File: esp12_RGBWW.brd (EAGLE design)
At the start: 53 x 47 mm, 36 parts, among them Q1 AOD2910SMD, Q2 AOD2910SMD, Q3 AOD2910SMD, Q4 AOD2910SMD, Q5 AOD2910SMD, U1 TPS5410DR

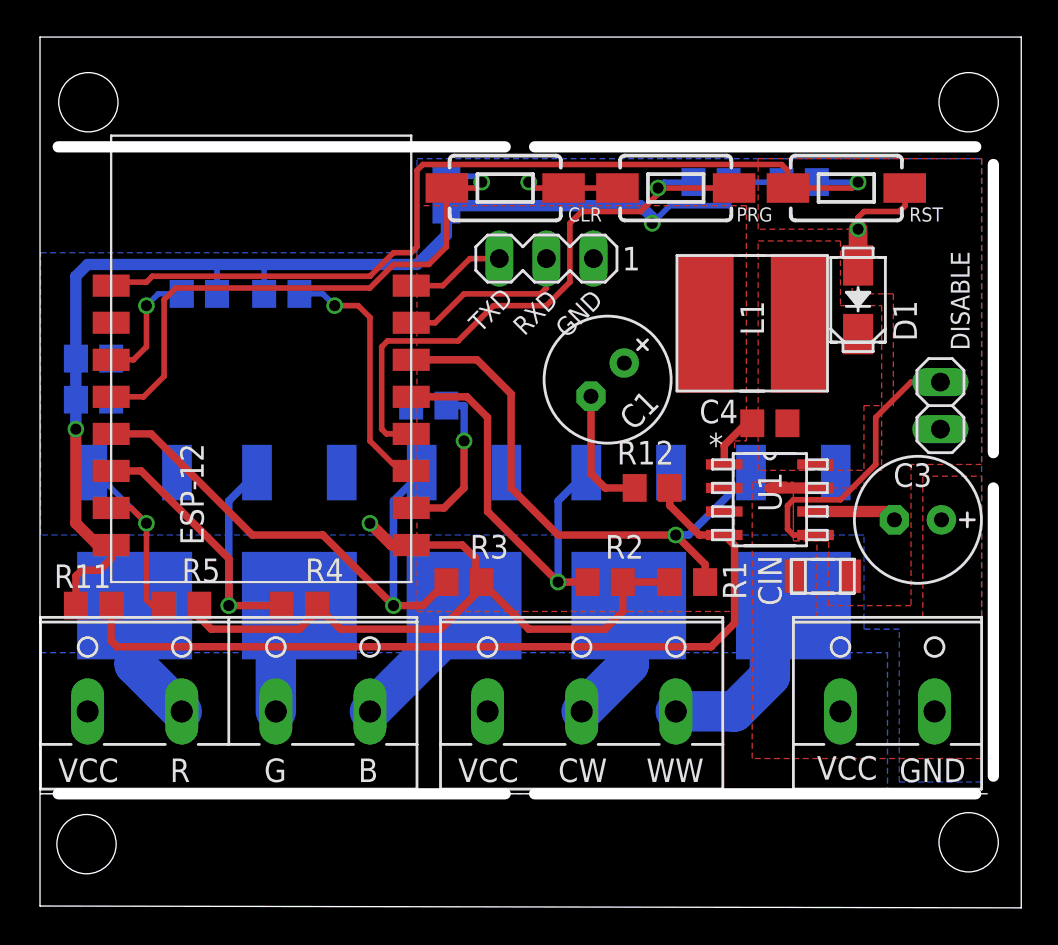
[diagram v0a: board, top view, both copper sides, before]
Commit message: minor routing changes
updated a few minor routings (clr) and added some more copper areas (GND around DISABLE & D1)
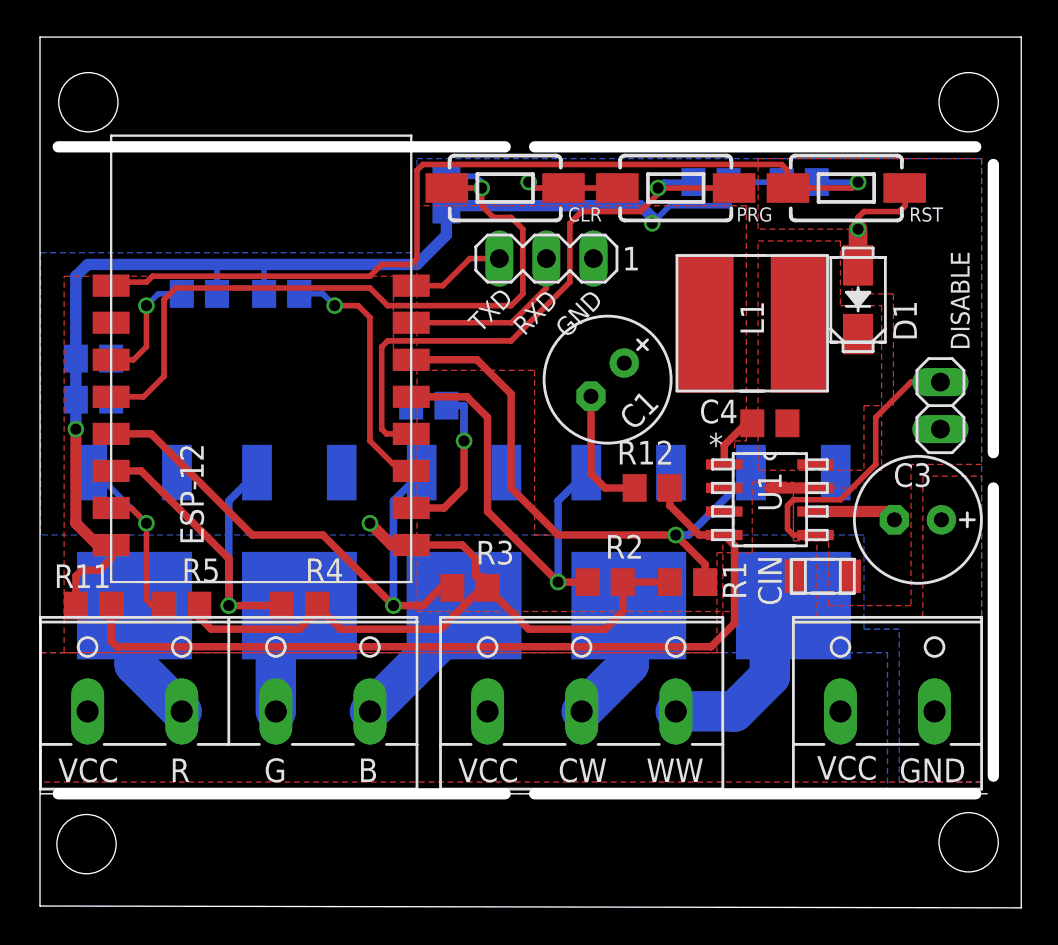
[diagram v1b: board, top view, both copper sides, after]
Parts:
- moved R3 0.45 mm to (21.9, 11.1)
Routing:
- net CLR_S: track 31.6 -> 39.4 mm
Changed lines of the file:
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@@
 <attribute name="NAME" x="29.21" y="12.7" size="1.27" layer="25"/>
 </element>
-<element name="R3" library="rcl" package="R0805" value="10k" x="21.59" y="11.43" smashed="yes">
-<attribute name="NAME" x="21.9075" y="12.7" size="1.27" layer="25"/>
+<element name="R3" library="rcl" package="R0805" value="10k" x="21.9075" y="11.1125" smashed="yes">
+<attribute name="NAME" x="22.225" y="12.3825" size="1.27" layer="25"/>
 </element>
 <element name="R4" library="rcl" package="R0805" value="10k" x="12.7" y="10.16" smashed="yes">
@@
 <wire x1="17.145" y1="19.685" x2="17.145" y2="24.13" width="0.3048" layer="1"/>
 <wire x1="17.145" y1="24.13" x2="17.4625" y2="24.4475" width="0.3048" layer="1"/>
-<wire x1="17.4625" y1="24.4475" x2="21.2725" y2="24.4475" width="0.3048" layer="1"/>
+<wire x1="17.4625" y1="24.4475" x2="24.13" y2="24.4475" width="0.3048" layer="1"/>
 <wire x1="27.305" y1="27.6225" x2="27.305" y2="30.7975" width="0.3048" layer="1"/>
 <wire x1="27.305" y1="30.7975" x2="27.94" y2="31.4325" width="0.3048" layer="1"/>
@@
 <wire x1="32.385" y1="33.02" x2="32.0675" y2="32.7025" width="0.3048" layer="16"/>
 <wire x1="36.17" y1="32.7025" x2="32.0675" y2="32.7025" width="0.3048" layer="1"/>
-<wire x1="21.2725" y1="24.4475" x2="23.1775" y2="26.3525" width="0.3048" layer="1"/>
-<wire x1="23.1775" y1="26.3525" x2="26.035" y2="26.3525" width="0.3048" layer="1"/>
-<wire x1="26.035" y1="26.3525" x2="27.305" y2="27.6225" width="0.3048" layer="1"/>
+<wire x1="24.13" y1="24.4475" x2="27.305" y2="27.6225" width="0.3048" layer="1"/>
 </signal>
 <signal name="GND">
@@
 <vertex x="-1.27" y="13.97"/>
 </polygon>
-<wire x1="22.54" y1="11.75" x2="22.54" y2="11.43" width="0.4064" layer="1"/>
-<wire x1="22.54" y1="11.43" x2="22.54" y2="11.11" width="0.4064" layer="1"/>
+<wire x1="22.54" y1="11.75" x2="22.8575" y2="11.1125" width="0.4064" layer="1"/>
+<wire x1="22.8575" y1="11.1125" x2="22.54" y2="11.11" width="0.4064" layer="1"/>
 <wire x1="22.54" y1="11.11" x2="20.32" y2="8.89" width="0.4064" layer="1"/>
 <wire x1="20.32" y1="8.89" x2="14.92" y2="8.89" width="0.4064" layer="1"/>
-<wire x1="22.54" y1="11.43" x2="22.86" y2="11.43" width="0.4064" layer="1"/>
+<wire x1="22.8575" y1="11.1125" x2="22.86" y2="11.43" width="0.4064" layer="1"/>
 <contactref element="VCC" pad="2"/>
 <contactref element="PROG" pad="1"/>
 <via x="16.51" y="14.605" extent="1-16" drill="0.6"/>
-<wire x1="25.08" y1="8.89" x2="22.54" y2="11.43" width="0.4064" layer="1"/>
+<wire x1="25.08" y1="8.89" x2="22.8575" y2="11.1125" width="0.4064" layer="1"/>
 <wire x1="18.74" y1="13.43" x2="21.495" y2="13.43" width="0.4064" layer="1"/>
 <wire x1="21.495" y1="13.43" x2="22.225" y2="12.7" width="0.4064" layer="1"/>
 <wire x1="22.225" y1="12.7" x2="22.225" y2="11.745" width="0.4064" layer="1"/>
-<wire x1="22.225" y1="11.745" x2="22.54" y2="11.43" width="0.4064" layer="1"/>
+<wire x1="22.225" y1="11.745" x2="22.8575" y2="11.1125" width="0.4064" layer="1"/>
 <wire x1="14.92" y1="8.89" x2="13.65" y2="10.16" width="0.4064" layer="1"/>
 <wire x1="13.65" y1="10.16" x2="13.65" y2="9.84" width="0.4064" layer="1"/>
@@
 <wire x1="40.5638" y1="15.24" x2="44.37295625" y2="15.24" width="0.6096" layer="1"/>
 <wire x1="44.37295625" y1="15.24" x2="44.821971875" y2="14.790984375" width="0.6096" layer="1"/>
+<polygon width="0.4064" layer="1">
+<vertex x="0" y="27.94"/>
+<vertex x="17.78" y="27.94"/>
+<vertex x="17.78" y="22.86"/>
+<vertex x="25.4" y="22.86"/>
+<vertex x="25.4" y="13.97"/>
+<vertex x="35.56" y="13.97"/>
+<vertex x="35.56" y="7.62"/>
+<vertex x="0" y="7.62"/>
+</polygon>
 </signal>
 <signal name="RST_S" class="5">
@@
 <wire x1="2.7325" y1="27.6225" x2="2.54" y2="27.43" width="0.3048" layer="1"/>
 <wire x1="40.6375" y1="33.02" x2="42.8625" y2="33.02" width="0.3048" layer="16"/>
-<wire x1="16.51" y1="27.94" x2="17.78" y2="29.21" width="0.3048" layer="1"/>
-<wire x1="17.78" y1="29.21" x2="18.7325" y2="29.21" width="0.3048" layer="1"/>
-<wire x1="18.7325" y1="29.21" x2="19.05" y2="29.5275" width="0.3048" layer="1"/>
 <wire x1="39.0775" y1="32.7025" x2="42.545" y2="32.7025" width="0.3048" layer="1"/>
 <wire x1="42.545" y1="32.7025" x2="42.8625" y2="33.02" width="0.3048" layer="1"/>
-<wire x1="19.05" y1="29.5275" x2="19.05" y2="33.655" width="0.3048" layer="1"/>
 <wire x1="19.05" y1="33.655" x2="19.3675" y2="33.9725" width="0.3048" layer="1"/>
 <wire x1="19.3675" y1="33.9725" x2="38.735" y2="33.9725" width="0.3048" layer="1"/>
@@
 <wire x1="39.0525" y1="33.655" x2="39.0525" y2="32.7275" width="0.3048" layer="1"/>
 <wire x1="39.0525" y1="32.7275" x2="39.0775" y2="32.7025" width="0.3048" layer="1"/>
+<wire x1="16.51" y1="27.94" x2="17.145" y2="28.575" width="0.3048" layer="1"/>
+<wire x1="17.145" y1="28.575" x2="18.7325" y2="28.575" width="0.3048" layer="1"/>
+<wire x1="18.7325" y1="28.575" x2="19.05" y2="28.8925" width="0.3048" layer="1"/>
+<wire x1="19.05" y1="28.8925" x2="19.05" y2="33.655" width="0.3048" layer="1"/>
 </signal>
 <signal name="RXD">
 <contactref element="ESP-12" pad="7"/>
 <contactref element="PROG" pad="2"/>
-<wire x1="18.74" y1="25.43" x2="20.0325" y2="25.43" width="0.3048" layer="1"/>
-<wire x1="20.0325" y1="25.43" x2="21.59" y2="26.9875" width="0.3048" layer="1"/>
-<wire x1="21.59" y1="26.9875" x2="25.7175" y2="26.9875" width="0.3048" layer="1"/>
-<wire x1="25.7175" y1="26.9875" x2="26.035" y2="27.305" width="0.3048" layer="1"/>
+<wire x1="18.74" y1="25.43" x2="24.16" y2="25.43" width="0.3048" layer="1"/>
+<wire x1="24.16" y1="25.43" x2="26.035" y2="27.305" width="0.3048" layer="1"/>
 <wire x1="26.035" y1="27.305" x2="26.035" y2="28.8925" width="0.3048" layer="1"/>
 </signal>
@@
 <contactref element="Q3" pad="1"/>
 <via x="17.78" y="10.16" extent="1-16" drill="0.6"/>
-<wire x1="20.64" y1="11.43" x2="19.37" y2="10.16" width="0.4064" layer="1"/>
 <wire x1="19.37" y1="10.16" x2="17.78" y2="10.16" width="0.4064" layer="1"/>
 <wire x1="10.16" y1="13.97" x2="4.7" y2="19.43" width="0.4064" layer="1"/>
@@
 <wire x1="17.78" y1="10.16" x2="17.78" y2="15.816" width="0.4064" layer="16"/>
 <wire x1="17.78" y1="15.816" x2="19.304" y2="17.34" width="0.4064" layer="16"/>
+<wire x1="19.37" y1="10.16" x2="19.37" y2="10.1625" width="0.4064" layer="1"/>
+<wire x1="19.37" y1="10.1625" x2="20.32" y2="11.1125" width="0.4064" layer="1"/>
+<wire x1="20.32" y1="11.1125" x2="20.9575" y2="11.1125" width="0.4064" layer="1"/>
 </signal>
 <signal name="RGB-G">
@@
 <vertex x="46.355" y="17.145"/>
 <vertex x="49.53" y="17.145"/>
-<vertex x="49.53" y="1.905"/>
-<vertex x="37.1475" y="1.905"/>
+<vertex x="49.53" y="0.635"/>
+<vertex x="-1.27" y="0.635"/>
+<vertex x="-1.27" y="7.62"/>
+<vertex x="35.2425" y="7.62"/>
+<vertex x="35.2425" y="13.0175"/>
+<vertex x="37.1475" y="13.0175"/>
 </polygon>
 <wire x1="40.5638" y1="16.51" x2="38.1" y2="16.51" width="0.6096" layer="1"/>
@@
 <contactref element="CLR" pad="2"/>
 <wire x1="2.38" y1="21.59" x2="2.54" y2="21.43" width="0.3048" layer="1"/>
-<wire x1="20.6375" y1="32.995" x2="20.6625" y2="32.7025" width="0.3048" layer="1"/>
-<via x="22.5425" y="33.02" extent="1-16" drill="0.6"/>
+<via x="22.5425" y="32.7025" extent="1-16" drill="0.6"/>
 <wire x1="20.6375" y1="33.335" x2="22.2275" y2="33.335" width="0.3048" layer="16"/>
-<wire x1="22.2275" y1="33.335" x2="22.5425" y2="33.02" width="0.3048" layer="16"/>
 <wire x1="2.54" y1="21.43" x2="4.285" y2="21.43" width="0.3048" layer="1"/>
 <wire x1="4.285" y1="21.43" x2="5.3975" y2="22.5425" width="0.3048" layer="1"/>
@@
 <wire x1="6.0325" y1="27.305" x2="5.3975" y2="26.67" width="0.3048" layer="1"/>
 <wire x1="5.3975" y1="26.67" x2="5.3975" y2="22.5425" width="0.3048" layer="1"/>
-<wire x1="16.51" y1="27.305" x2="17.78" y2="28.575" width="0.3048" layer="1"/>
-<wire x1="17.78" y1="28.575" x2="19.685" y2="28.575" width="0.3048" layer="1"/>
-<wire x1="19.685" y1="28.575" x2="20.6375" y2="29.5275" width="0.3048" layer="1"/>
-<wire x1="20.6375" y1="29.5275" x2="20.6375" y2="32.6775" width="0.3048" layer="1"/>
 <wire x1="20.6375" y1="32.6775" x2="20.6625" y2="32.7025" width="0.3048" layer="1"/>
-<wire x1="20.6625" y1="32.7025" x2="22.225" y2="32.7025" width="0.3048" layer="1"/>
-<wire x1="22.225" y1="32.7025" x2="22.5425" y2="33.02" width="0.3048" layer="1"/>
+<wire x1="16.51" y1="27.305" x2="17.4625" y2="26.3525" width="0.3048" layer="1"/>
+<wire x1="17.4625" y1="26.3525" x2="24.13" y2="26.3525" width="0.3048" layer="1"/>
+<wire x1="24.13" y1="26.3525" x2="24.765" y2="26.9875" width="0.3048" layer="1"/>
+<wire x1="24.765" y1="26.9875" x2="24.765" y2="30.48" width="0.3048" layer="1"/>
+<wire x1="22.2275" y1="33.335" x2="22.5425" y2="33.02" width="0.3048" layer="16"/>
+<wire x1="22.5425" y1="33.02" x2="22.5425" y2="32.7025" width="0.3048" layer="16"/>
+<wire x1="20.6625" y1="32.7025" x2="22.5425" y2="32.7025" width="0.3048" layer="1"/>
+<wire x1="22.5425" y1="32.7025" x2="22.5425" y2="31.75" width="0.3048" layer="1"/>
+<wire x1="22.5425" y1="31.75" x2="23.1775" y2="31.115" width="0.3048" layer="1"/>
+<wire x1="23.1775" y1="31.115" x2="24.13" y2="31.115" width="0.3048" layer="1"/>
+<wire x1="24.13" y1="31.115" x2="24.765" y2="30.48" width="0.3048" layer="1"/>
 </signal>
 <signal name="PH">

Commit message: fixed a pretty embarassing error
I had one ground trace clip one of the PWM output pads.
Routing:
- net GND: track 65.4 -> 52.4 mm
- net B: track 7.82 -> 7.18 mm
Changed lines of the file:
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@@
 <vertex x="-1.27" y="13.97"/>
 </polygon>
-<wire x1="22.54" y1="11.75" x2="22.8575" y2="11.1125" width="0.4064" layer="1"/>
-<wire x1="22.8575" y1="11.1125" x2="22.54" y2="11.11" width="0.4064" layer="1"/>
-<wire x1="22.54" y1="11.11" x2="20.32" y2="8.89" width="0.4064" layer="1"/>
 <wire x1="20.32" y1="8.89" x2="14.92" y2="8.89" width="0.4064" layer="1"/>
 <wire x1="22.8575" y1="11.1125" x2="22.86" y2="11.43" width="0.4064" layer="1"/>
@@
 <contactref element="PROG" pad="1"/>
 <via x="16.51" y="14.605" extent="1-16" drill="0.6"/>
-<wire x1="25.08" y1="8.89" x2="22.8575" y2="11.1125" width="0.4064" layer="1"/>
-<wire x1="18.74" y1="13.43" x2="21.495" y2="13.43" width="0.4064" layer="1"/>
-<wire x1="21.495" y1="13.43" x2="22.225" y2="12.7" width="0.4064" layer="1"/>
-<wire x1="22.225" y1="12.7" x2="22.225" y2="11.745" width="0.4064" layer="1"/>
-<wire x1="22.225" y1="11.745" x2="22.8575" y2="11.1125" width="0.4064" layer="1"/>
 <wire x1="14.92" y1="8.89" x2="13.65" y2="10.16" width="0.4064" layer="1"/>
 <wire x1="13.65" y1="10.16" x2="13.65" y2="9.84" width="0.4064" layer="1"/>
@@
 <contactref element="RGB" pad="4"/>
 <contactref element="Q3" pad="4"/>
-<wire x1="21.59" y1="10.16" x2="21.59" y2="9.525" width="2.1844" layer="16"/>
 <wire x1="21.59" y1="9.525" x2="16.51" y2="4.445" width="2.1844" layer="16"/>
+<wire x1="21.59" y1="9.525" x2="21.59" y2="10.16" width="0" layer="19" extent="16-16"/>
 </signal>
 <signal name="N$4">
@@
 </signal>
 </signals>
-<errors>
-</errors>
 </board>
 </drawing>

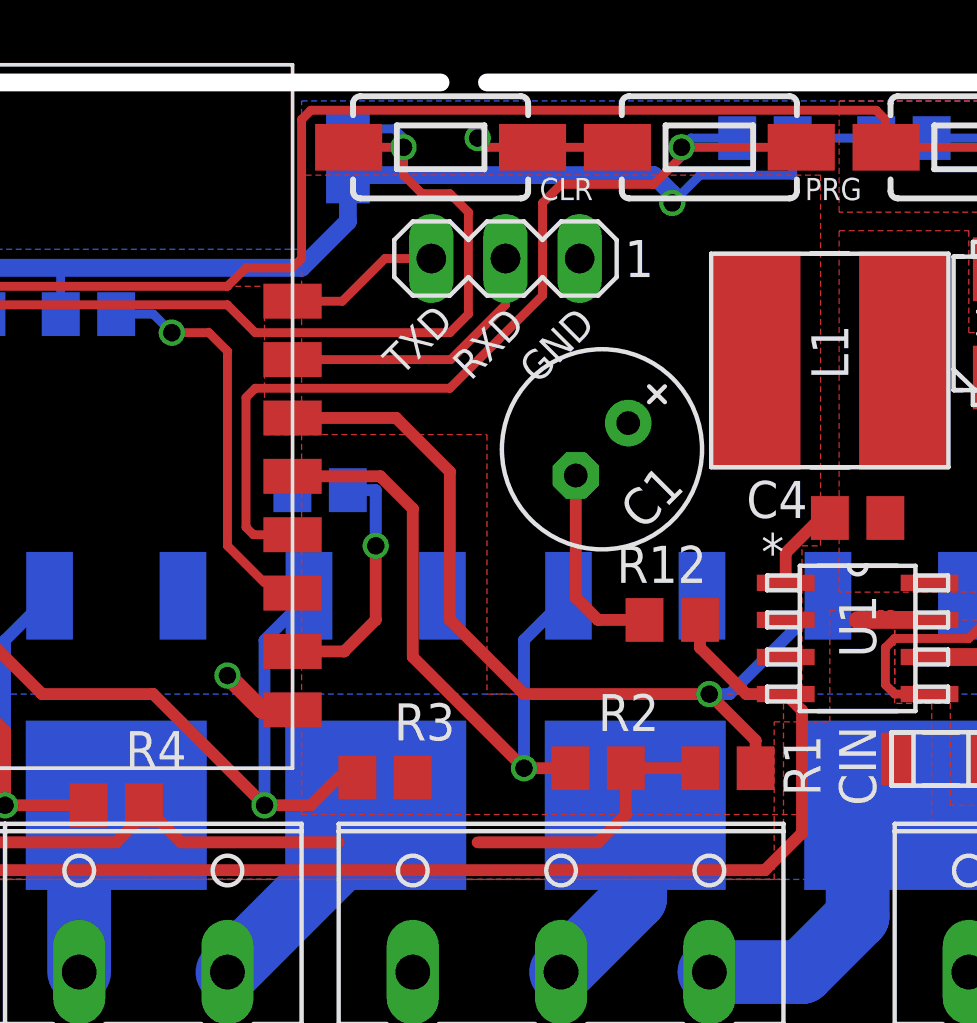
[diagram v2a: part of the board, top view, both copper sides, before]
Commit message: minor change
one of the GND traces (between R2 and R3) underneath the top ground plane was not connected - doesn't make a change in the final board since it's one copper layer anyway.
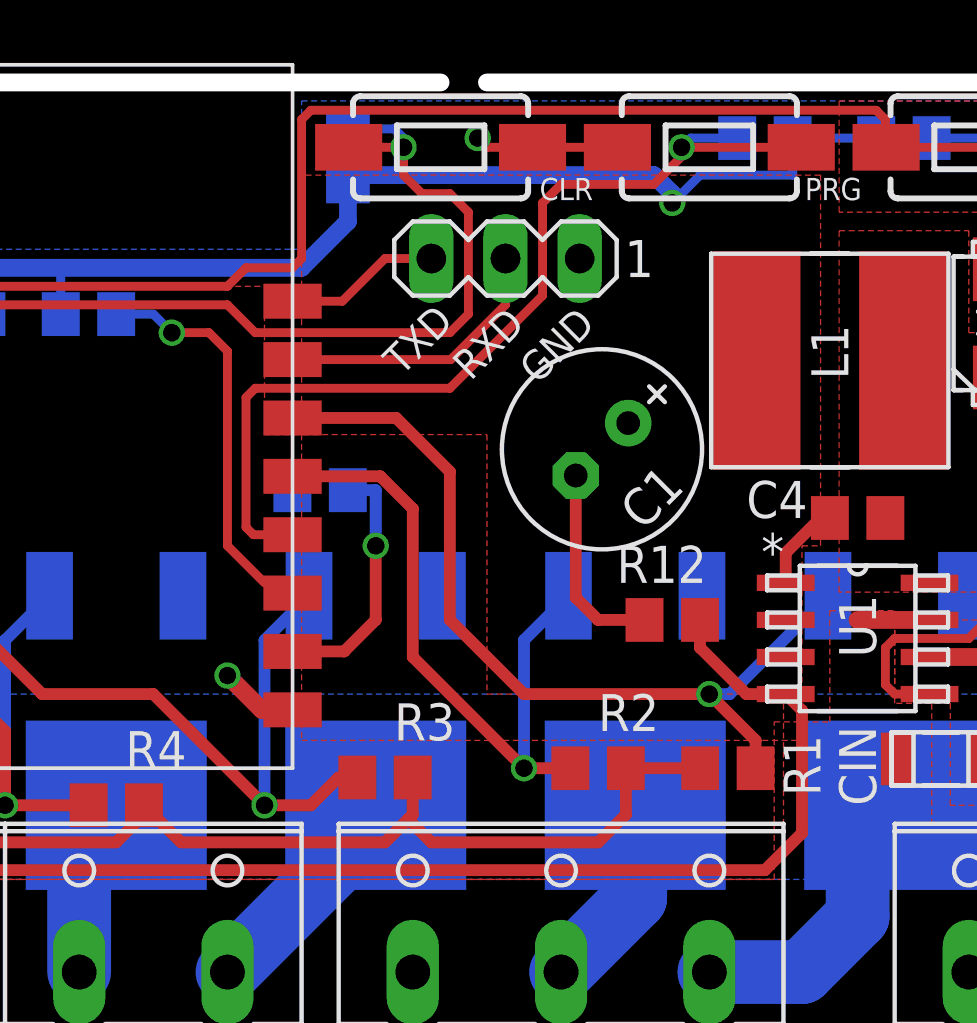
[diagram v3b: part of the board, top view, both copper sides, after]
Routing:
- net GND: track 52.4 -> 59.3 mm
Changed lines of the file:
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@@
 <vertex x="-1.27" y="13.97"/>
 </polygon>
-<wire x1="20.32" y1="8.89" x2="14.92" y2="8.89" width="0.4064" layer="1"/>
 <wire x1="22.8575" y1="11.1125" x2="22.86" y2="11.43" width="0.4064" layer="1"/>
 <contactref element="VCC" pad="2"/>
@@
 <wire x1="42.8625" y1="28.5242" x2="42.8625" y2="30.48" width="1.016" layer="1"/>
 <wire x1="30.16" y1="11.43" x2="32.705" y2="11.43" width="0.4064" layer="1"/>
-<wire x1="25.08" y1="8.89" x2="29.21" y2="8.89" width="0.4064" layer="1"/>
-<wire x1="29.21" y1="8.89" x2="30.1625" y2="9.8425" width="0.4064" layer="1"/>
-<wire x1="30.1625" y1="9.8425" x2="30.1625" y2="11.4275" width="0.4064" layer="1"/>
 <wire x1="30.1625" y1="11.4275" x2="30.16" y2="11.43" width="0.4064" layer="1"/>
 <wire x1="45.4025" y1="31.75" x2="45.4025" y2="32.995" width="0.3048" layer="1"/>
@@
 <vertex x="0" y="7.62"/>
 </polygon>
+<wire x1="14.92" y1="8.89" x2="21.9075" y2="8.89" width="0.4064" layer="1"/>
+<wire x1="21.9075" y1="8.89" x2="22.70125" y2="9.68375" width="0.4064" layer="1"/>
+<wire x1="22.70125" y1="9.68375" x2="22.8575" y2="9.84" width="0.4064" layer="1"/>
+<wire x1="22.8575" y1="9.84" x2="22.8575" y2="11.1125" width="0.4064" layer="1"/>
+<wire x1="30.1625" y1="11.4275" x2="30.1625" y2="9.8425" width="0.4064" layer="1"/>
+<wire x1="30.1625" y1="9.8425" x2="29.21" y2="8.89" width="0.4064" layer="1"/>
+<wire x1="29.21" y1="8.89" x2="23.495" y2="8.89" width="0.4064" layer="1"/>
+<wire x1="23.495" y1="8.89" x2="22.70125" y2="9.68375" width="0.4064" layer="1"/>
 </signal>
 <signal name="RST_S" class="5">
@@
 <wire x1="10.7975" y1="28.5725" x2="10.795" y2="28.575" width="0.3048" layer="16"/>
 <polygon width="0.3048" layer="1">
-<vertex x="36.195" y="9.8425"/>
+<vertex x="36.195" y="12.3825"/>
 <vertex x="36.195" y="19.05"/>
 <vertex x="36.83" y="19.05"/>
 <vertex x="36.83" y="31.75"/>
 <vertex x="19.05" y="31.75"/>
-<vertex x="19.05" y="9.8425"/>
+<vertex x="19.05" y="12.3825"/>
 </polygon>
 <wire x1="35.875" y1="33.02" x2="38.7375" y2="33.02" width="0.3048" layer="16"/>
